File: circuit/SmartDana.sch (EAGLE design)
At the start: 18 parts

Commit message: 回転灯動作確認
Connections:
- net N$10 renamed LIGHT_LAMP
- net N$9 renamed LIGHT_MOTOR
- removed net N$11: ARDUINO_NANO1.D6, LIGHT.4
- new net LIGHT_PWM: ARDUINO_NANO1.D3, LIGHT.4
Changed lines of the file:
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@@
 </segment>
 </net>
-<net name="N$9" class="0">
+<net name="LIGHT_MOTOR" class="0">
 <segment>
 <wire x1="-35.56" y1="50.8" x2="-35.56" y2="33.02" width="0.1524" layer="91"/>
@@
 <wire x1="-35.56" y1="50.8" x2="15.24" y2="50.8" width="0.1524" layer="91"/>
 <pinref part="ARDUINO_NANO1" gate="G$1" pin="D7"/>
+<label x="-30.48" y="50.8" size="1.778" layer="95"/>
 </segment>
 </net>
-<net name="N$10" class="0">
+<net name="LIGHT_LAMP" class="0">
 <segment>
 <pinref part="RELAY_C" gate="A" pin="3"/>
@@
 <pinref part="ARDUINO_NANO1" gate="G$1" pin="D8"/>
 <wire x1="-33.02" y1="48.26" x2="15.24" y2="48.26" width="0.1524" layer="91"/>
+<label x="-30.48" y="48.26" size="1.778" layer="95"/>
 </segment>
 </net>
-<net name="N$11" class="0">
+<net name="LIGHT_PWM" class="0">
 <segment>
 <wire x1="-55.88" y1="33.02" x2="-66.04" y2="33.02" width="0.1524" layer="91"/>
 <pinref part="LIGHT" gate="A" pin="4"/>
-<wire x1="-55.88" y1="53.34" x2="-55.88" y2="33.02" width="0.1524" layer="91"/>
-<pinref part="ARDUINO_NANO1" gate="G$1" pin="D6"/>
-<wire x1="-55.88" y1="53.34" x2="15.24" y2="53.34" width="0.1524" layer="91"/>
+<wire x1="-55.88" y1="60.96" x2="-55.88" y2="33.02" width="0.1524" layer="91"/>
+<pinref part="ARDUINO_NANO1" gate="G$1" pin="D3"/>
+<wire x1="-55.88" y1="60.96" x2="15.24" y2="60.96" width="0.1524" layer="91"/>
+<label x="-30.48" y="60.96" size="1.778" layer="95"/>
 </segment>
 </net>

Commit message: NodeMCU動作テスト中
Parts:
- removed R1: (no value), rcl:R-EU_0207/12
- added R9: (no value), rcl:R-EU_0207/12
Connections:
- removed net N$4: ARDUINO_NANO1.D11, R1.1
- new net N$1: ARDUINO_NANO1.D11, R9.1
- net MISO(SDO): now also ARDUINO_NANO1.D12; no longer R1.2
- net MOSI(SDI): now also R9.2; no longer ARDUINO_NANO1.D12
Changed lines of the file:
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@@
 <part name="GND6" library="supply1" library_urn="urn:adsk.eagle:library:371" deviceset="GND" device=""/>
 <part name="GND7" library="supply1" library_urn="urn:adsk.eagle:library:371" deviceset="GND" device=""/>
-<part name="R1" library="rcl" library_urn="urn:adsk.eagle:library:334" deviceset="R-EU_" device="0207/12" package3d_urn="urn:adsk.eagle:package:23489/1"/>
 <part name="R2" library="rcl" library_urn="urn:adsk.eagle:library:334" deviceset="R-EU_" device="0207/12" package3d_urn="urn:adsk.eagle:package:23489/1"/>
 <part name="R3" library="rcl" library_urn="urn:adsk.eagle:library:334" deviceset="R-EU_" device="0207/12" package3d_urn="urn:adsk.eagle:package:23489/1"/>
@@
 <part name="R7" library="rcl" library_urn="urn:adsk.eagle:library:334" deviceset="R-EU_" device="0207/12" package3d_urn="urn:adsk.eagle:package:23489/1"/>
 <part name="R8" library="rcl" library_urn="urn:adsk.eagle:library:334" deviceset="R-EU_" device="0207/12" package3d_urn="urn:adsk.eagle:package:23489/1"/>
+<part name="R9" library="rcl" library_urn="urn:adsk.eagle:library:334" deviceset="R-EU_" device="0207/12" package3d_urn="urn:adsk.eagle:package:23489/1"/>
 </parts>
 <sheets>
@@
 <instance part="GND6" gate="1" x="-71.12" y="53.34"/>
 <instance part="GND7" gate="1" x="109.22" y="5.08"/>
-<instance part="R1" gate="G$1" x="86.36" y="17.78"/>
 <instance part="R2" gate="G$1" x="86.36" y="12.7"/>
 <instance part="R3" gate="G$1" x="86.36" y="20.32"/>
@@
 <instance part="R7" gate="G$1" x="81.28" y="-55.88"/>
 <instance part="R8" gate="G$1" x="81.28" y="-58.42"/>
+<instance part="R9" gate="G$1" x="86.36" y="15.24"/>
 </instances>
 <busses>
@@
 <net name="MOSI(SDI)" class="0">
 <segment>
-<pinref part="ARDUINO_NANO1" gate="G$1" pin="D12"/>
-<wire x1="15.24" y1="38.1" x2="10.16" y2="38.1" width="0.1524" layer="91"/>
-<wire x1="10.16" y1="38.1" x2="10.16" y2="15.24" width="0.1524" layer="91"/>
-<wire x1="10.16" y1="15.24" x2="93.98" y2="15.24" width="0.1524" layer="91"/>
 <pinref part="PS2_CON" gate="A" pin="4"/>
 <label x="104.14" y="15.24" size="1.778" layer="95"/>
+<wire x1="91.44" y1="15.24" x2="93.98" y2="15.24" width="0.1524" layer="91"/>
 <wire x1="93.98" y1="15.24" x2="121.92" y2="15.24" width="0.1524" layer="91"/>
 <wire x1="93.98" y1="15.24" x2="93.98" y2="-17.78" width="0.1524" layer="91"/>
@@
 <junction x="93.98" y="-17.78"/>
 <label x="104.14" y="-50.8" size="1.778" layer="95"/>
-</segment>
-</net>
-<net name="N$4" class="0">
-<segment>
-<pinref part="ARDUINO_NANO1" gate="G$1" pin="D11"/>
-<wire x1="15.24" y1="40.64" x2="7.62" y2="40.64" width="0.1524" layer="91"/>
-<wire x1="7.62" y1="40.64" x2="7.62" y2="17.78" width="0.1524" layer="91"/>
-<wire x1="7.62" y1="17.78" x2="81.28" y2="17.78" width="0.1524" layer="91"/>
-<pinref part="R1" gate="G$1" pin="1"/>
+<pinref part="R9" gate="G$1" pin="2"/>
 </segment>
 </net>
@@
 <net name="MISO(SDO)" class="0">
 <segment>
-<pinref part="R1" gate="G$1" pin="2"/>
 <pinref part="PS2_CON" gate="A" pin="3"/>
-<wire x1="91.44" y1="17.78" x2="96.52" y2="17.78" width="0.1524" layer="91"/>
 <label x="104.14" y="17.78" size="1.778" layer="95"/>
 <wire x1="96.52" y1="17.78" x2="121.92" y2="17.78" width="0.1524" layer="91"/>
@@
 <junction x="96.52" y="-15.24"/>
 <label x="104.14" y="-48.26" size="1.778" layer="95"/>
+<wire x1="12.7" y1="17.78" x2="96.52" y2="17.78" width="0.1524" layer="91"/>
+<wire x1="12.7" y1="17.78" x2="12.7" y2="38.1" width="0.1524" layer="91"/>
+<pinref part="ARDUINO_NANO1" gate="G$1" pin="D12"/>
+<wire x1="12.7" y1="38.1" x2="15.24" y2="38.1" width="0.1524" layer="91"/>
 </segment>
 </net>
@@
 </segment>
 </net>
+<net name="N$1" class="0">
+<segment>
+<pinref part="ARDUINO_NANO1" gate="G$1" pin="D11"/>
+<wire x1="15.24" y1="40.64" x2="10.16" y2="40.64" width="0.1524" layer="91"/>
+<pinref part="R9" gate="G$1" pin="1"/>
+<wire x1="10.16" y1="40.64" x2="10.16" y2="15.24" width="0.1524" layer="91"/>
+<wire x1="10.16" y1="15.24" x2="81.28" y2="15.24" width="0.1524" layer="91"/>
+</segment>
+</net>

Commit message: パターン設計仮完了
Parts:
- removed JP1: (no value), pinhead:PINHD-1X9/90
- removed LIGHT: (no value), pinhead:PINHD-1X5/90
- removed RELAY: (no value), pinhead:PINHD-1X6
- removed RELAY_C: (no value), pinhead:PINHD-1X4/90
- added ARDUINO_POWER, SERVO_POWER: (no value), pinhead:PINHD-1X2
- added JP3: (no value), pinhead:PINHD-1X5
- added LCD: (no value), pinhead:PINHD-1X9
- LEAD_SW: device pinhead:PINHD-1X2/90 -> pinhead:PINHD-1X2
- PS2_CON: device pinhead:PINHD-1X6/90 -> pinhead:PINHD-1X6
- R2, R3, R4, R5, R6, R7, R8, R9: device rcl:R-EU_0207/12 -> rcl:R-EU_0204/7
- RASPI: device pinhead:PINHD-1X4/90 -> pinhead:PINHD-1X4
- RC_SERVO: device pinhead:PINHD-1X3/90 -> pinhead:PINHD-1X3
- RFID-RC522: device pinhead:PINHD-1X7/90 -> pinhead:PINHD-1X7
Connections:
- removed net +12V: RELAY.1, RELAY.4
- removed net N$3: LIGHT.2, RELAY.2
- removed net N$8: LIGHT.3, RELAY.5
- new net +4.1V: RC_SERVO.2, SERVO_POWER.1
- new net VCC: ARDUINO_NANO1.VIN, ARDUINO_POWER.1
- net +3V3: now also LCD.1, LCD.8; no longer JP1.1, JP1.8
- net +5V: now also JP3.1; no longer RC_SERVO.2, RELAY_C.1
- net DC: now also LCD.7; no longer JP1.7
- net GND: now also ARDUINO_POWER.2, JP3.5, LCD.9, SERVO_POWER.2; no longer JP1.9, LIGHT.1, LIGHT.5, RELAY_C.4
- net LIGHT_LAMP: now also JP3.2; no longer RELAY_C.3
- net LIGHT_MOTOR: now also JP3.3; no longer RELAY_C.2
- net LIGHT_PWM: now also JP3.4; no longer LIGHT.4
- net MISO(SDO): now also LCD.3; no longer JP1.3
- net MOSI(SDI): now also LCD.4; no longer JP1.4
- net RESET2: now also LCD.6; no longer JP1.6
- net SCK: now also LCD.2; no longer JP1.2
- net SS3: now also LCD.5; no longer JP1.5

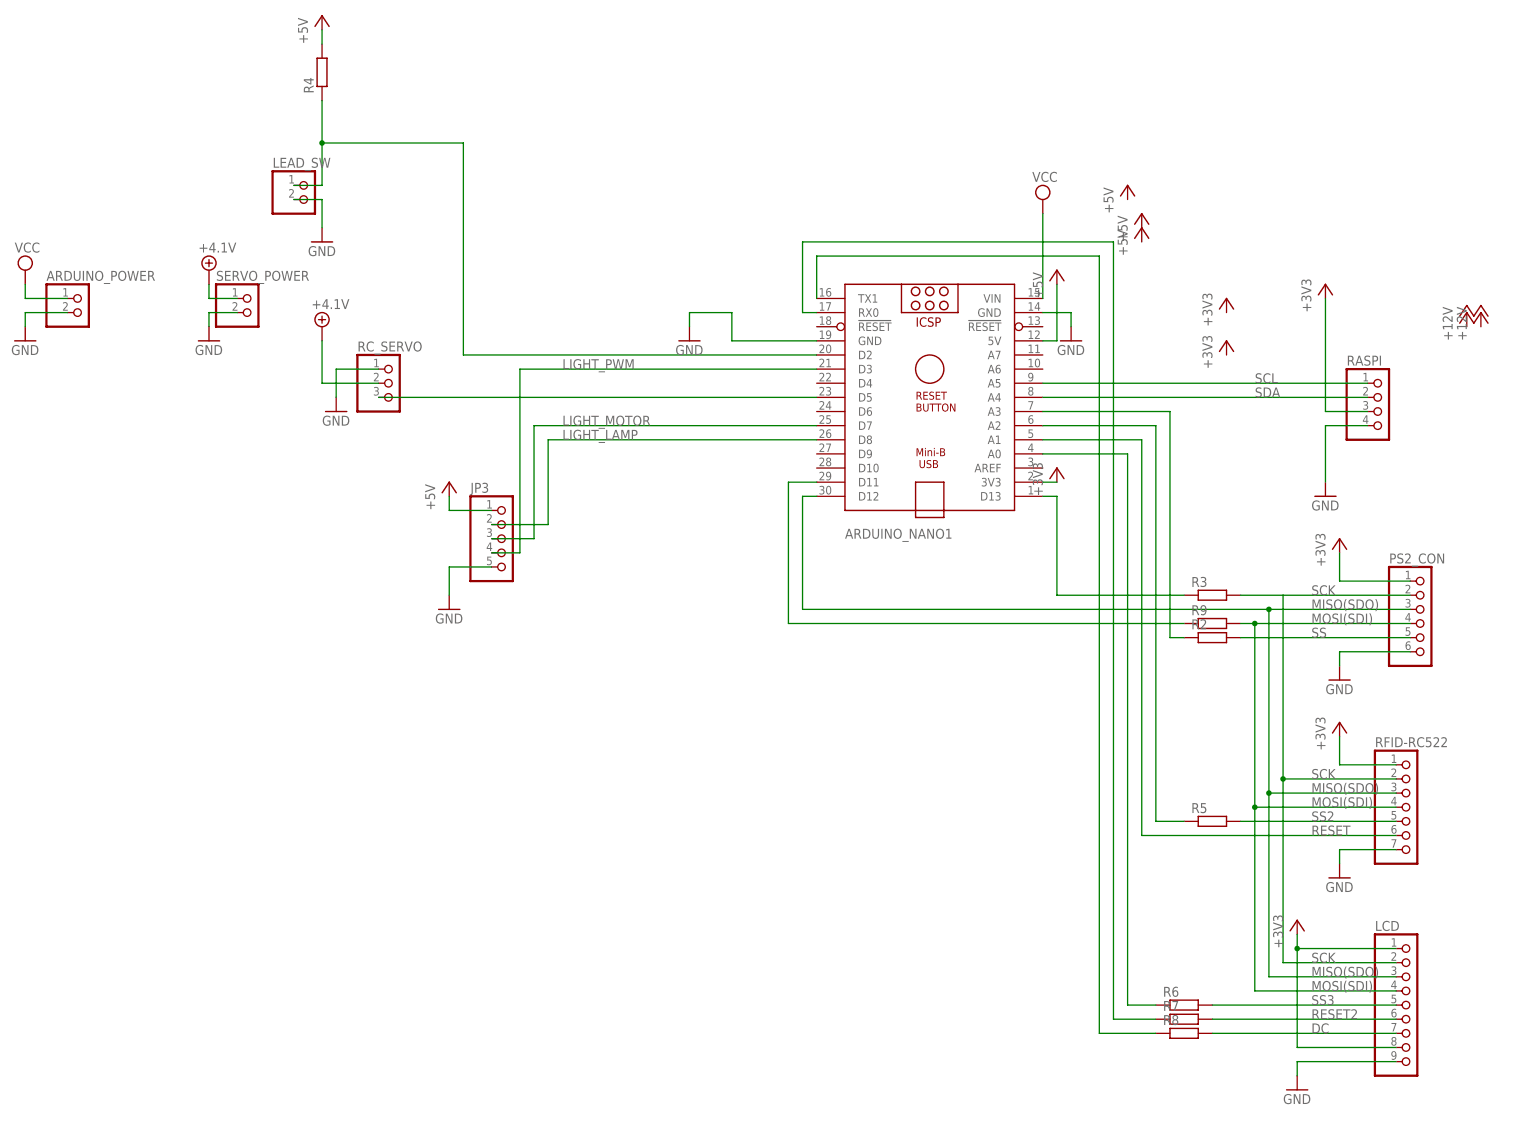
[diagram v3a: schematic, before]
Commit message: 体重をTCPで送信できた
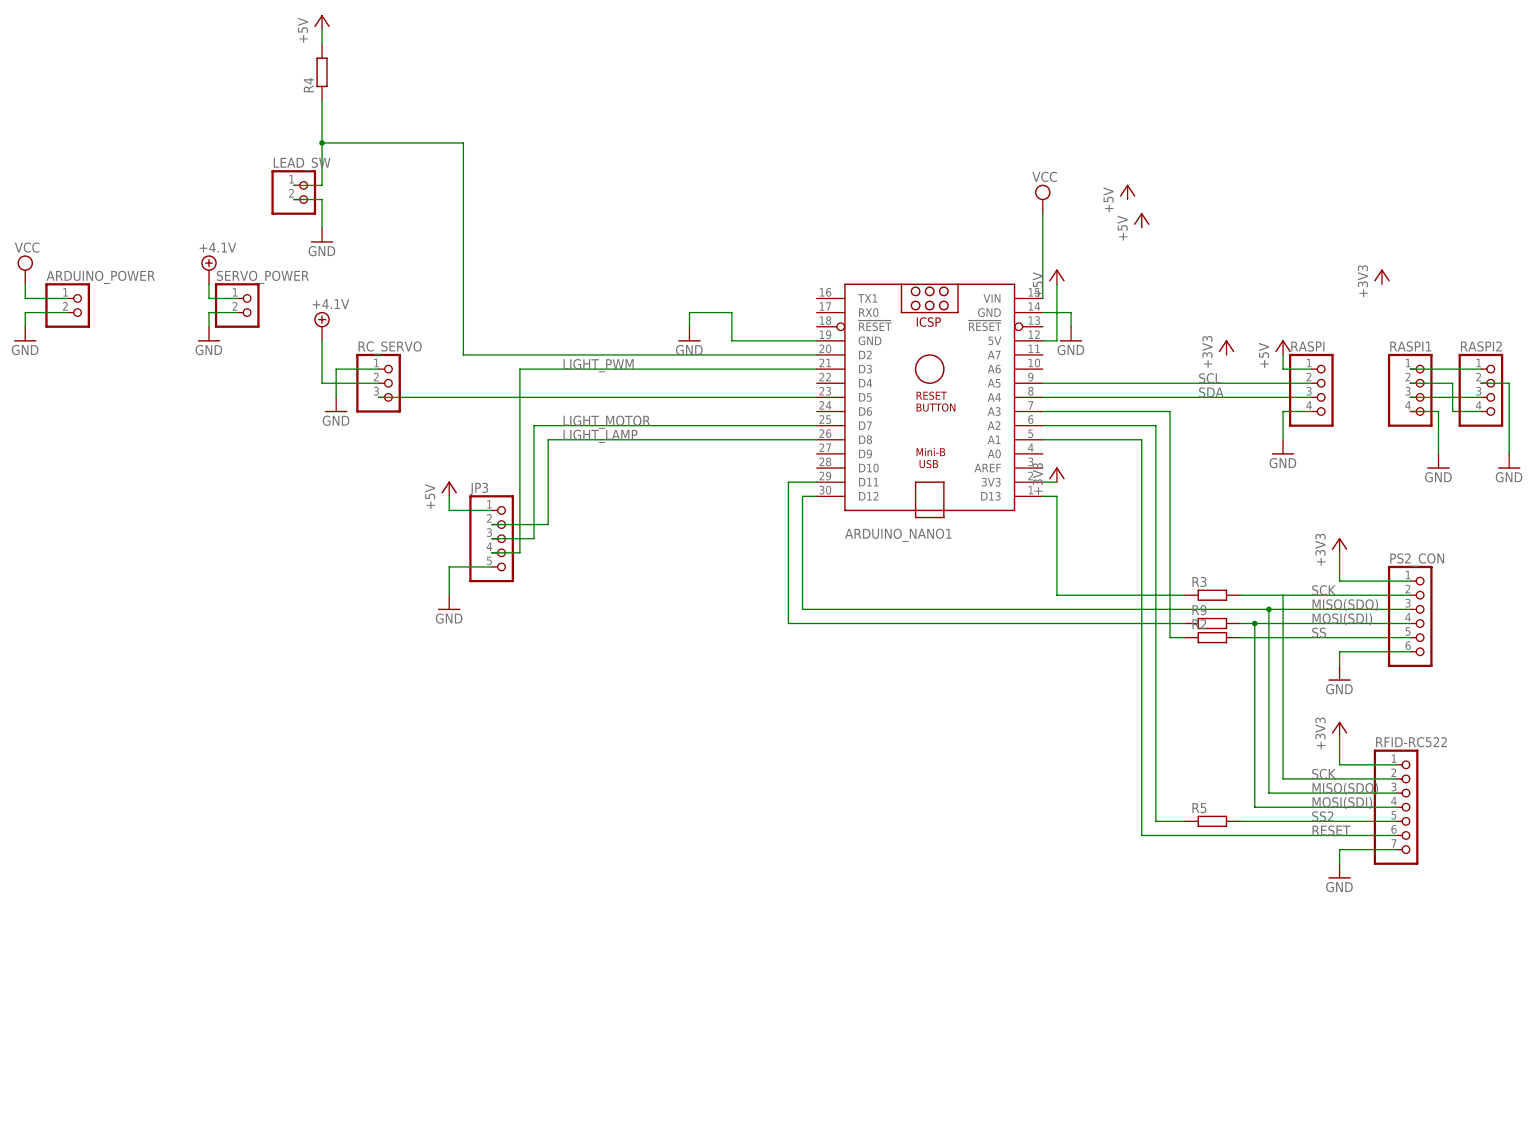
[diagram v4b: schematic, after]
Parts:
- removed LCD: (no value), pinhead:PINHD-1X9
- removed R6, R7, R8: (no value), rcl:R-EU_0204/7
- added RASPI1, RASPI2: (no value), pinhead:PINHD-1X4
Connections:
- removed net DC: LCD.7, R8.2
- removed net N$13: ARDUINO_NANO1.A0, R6.1
- removed net N$19: ARDUINO_NANO1.RX0, R7.1
- removed net N$20: ARDUINO_NANO1.TX1, R8.1
- removed net RESET2: LCD.6, R7.2
- removed net SS3: LCD.5, R6.2
- new net N$3: RASPI1.1, RASPI2.1
- new net N$8: RASPI1.2, RASPI2.4
- new net N$9: RASPI1.3, RASPI2.3
- net +3V3: no longer LCD.1, LCD.8, RASPI.3
- net +5V: now also RASPI.1
- net GND: now also RASPI1.4, RASPI2.2; no longer LCD.9
- net MISO(SDO): no longer LCD.3
- net MOSI(SDI): no longer LCD.4
- net SCK: no longer LCD.2
- net SCL: now also RASPI.2; no longer RASPI.1
- net SDA: now also RASPI.3; no longer RASPI.2
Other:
- moved on the sheet: RASPI
